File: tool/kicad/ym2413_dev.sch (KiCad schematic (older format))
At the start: 145 parts, among them J1 MICRO-USB-AB, K1 CONN_3, K2 CONN_3, P1 TEST_POINT, P10 TEST_POINT, P11 TEST_POINT, P12 TEST_POINT, P13 TEST_POINT, P14 TEST_POINT, P15 TEST_POINT, P16 TEST_POINT, P17 TEST_POINT, P18 TEST_POINT, P19 TEST_POINT, P2 TEST_POINT, P20 TEST_POINT, P21 TEST_POINT, P22 TEST_POINT, P23 TEST_POINT, P24 TEST_POINT, P25 TEST_POINT, P26 TEST_POINT, P27 TEST_POINT, P28 TEST_POINT, P29 TEST_POINT, P3 TEST_POINT, P30 CONN_3X2, P31 CONN_2, P32 CONN_2, P33 TEST_POINT, P34 TEST_POINT, P35 CONN_6, P37 TEST_POINT, P38 TEST_POINT, P4 TEST_POINT, P5 MIDI-IN, P6 TEST_POINT, P7 TEST_POINT, P8 TEST_POINT, P9 TEST_POINT, U1 SN74LVC2T45, U2 ST-USBLC6-2, U3 EFM32GG332, U4 YM2413, U5 LM386, U6 LM386, U7 ACPL-M21L, X1 48Mhz, X2 CRYSTAL

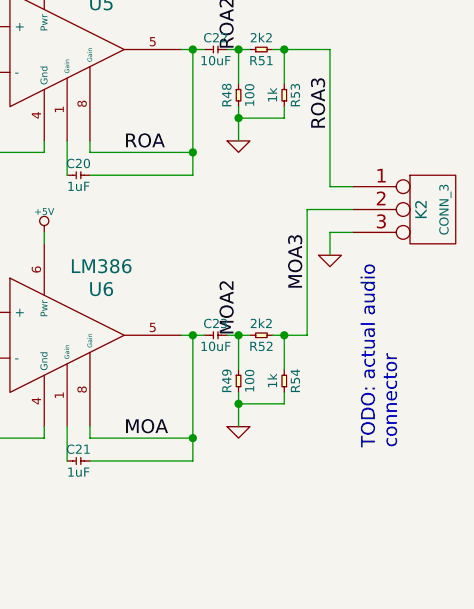
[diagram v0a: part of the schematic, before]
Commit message: fix audio footprint; add to board
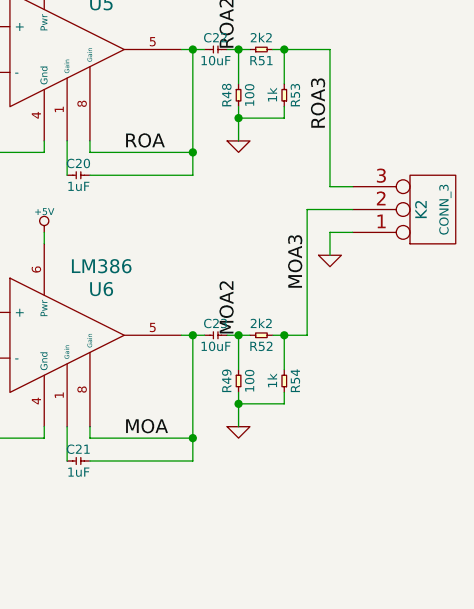
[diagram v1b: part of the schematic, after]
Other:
- note removed: "TODO: actual audio\nconnector"
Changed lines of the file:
@@
 F 3 "" H 10850 3950 60  0000 C CNN
 	1    10850 3950
-	1    0    0    -1
+	1    0    0    1
 $EndComp
 Wire Wire Line
@@
 Wire Wire Line
 	10400 4050 10400 4150
-Text Notes 10700 5000 1    60   ~ 0
-TODO: actual audio\nconnector
 $Comp
 L SN74LVC2T45 U1

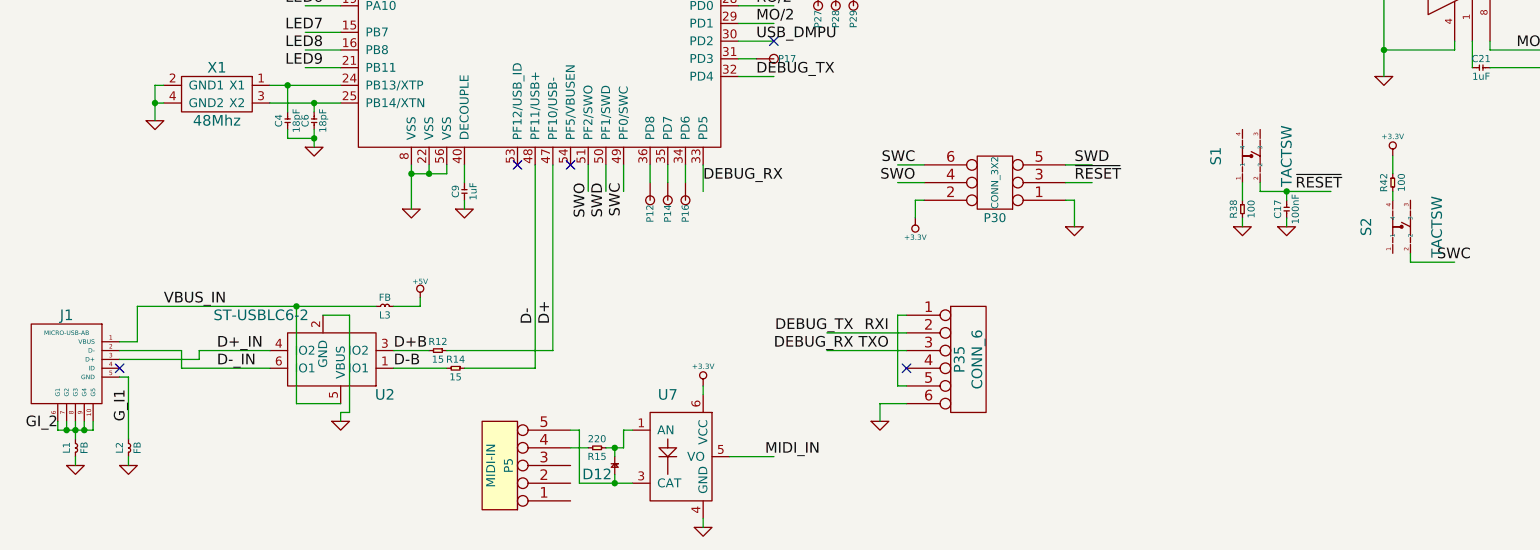
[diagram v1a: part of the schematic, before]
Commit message: ERC fixes
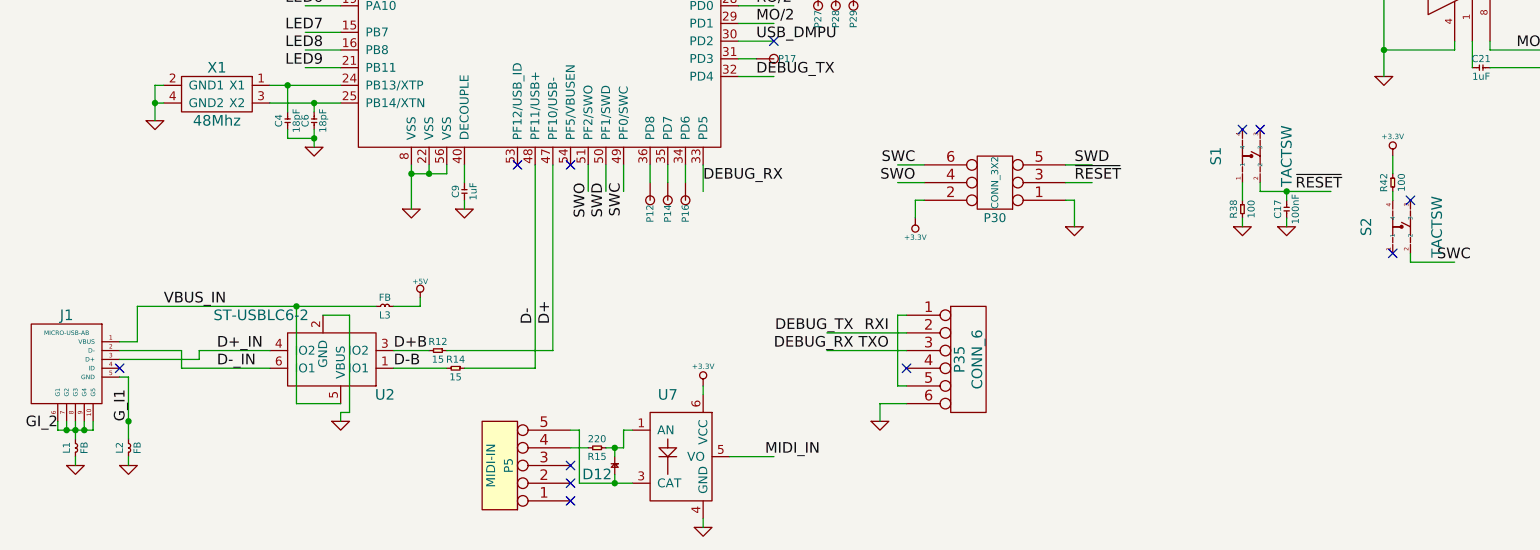
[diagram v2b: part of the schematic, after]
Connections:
- no-connect marks 5 -> 12
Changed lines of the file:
@@
 Wire Wire Line
 	5300 7250 5050 7250
+Connection ~ 1650 7050
+NoConn ~ 8800 6100
+NoConn ~ 8900 5800
+NoConn ~ 8050 5400
+NoConn ~ 7950 5400
+NoConn ~ 4150 7300
+NoConn ~ 4150 7400
+NoConn ~ 4150 7500
 $EndSCHEMATC

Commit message: work on 3V3 part
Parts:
- added C24: 4.7uF, symbol C
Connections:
- net labels added: DECOUPLE, SWCU, XTN, XTP, ~RESETD
- wire segments 356 -> 358
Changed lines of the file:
@@
 	4150 2550 4150 2500
 Wire Wire Line
-	4150 2500 4050 2500
+	4050 2500 4300 2500
 Connection ~ 4050 2500
 Wire Wire Line
@@
 NoConn ~ 4150 7400
 NoConn ~ 4150 7500
+Text Label 7950 5750 2    60   ~ 0
+~RESETD
+Text Label 8800 5800 2    60   ~ 0
+SWCU
+Text Label 2600 5150 0    60   ~ 0
+XTP
+Text Label 2600 5250 0    60   ~ 0
+XTN
+$Comp
+L C C24
+U 1 1 530648AC
+P 4300 2600
+F 0 "C24" H 4300 2650 40  0000 C CNN
+F 1 "4.7uF" H 4300 2550 40  0000 C CNN
+F 2 "" H 4300 2600 60  0000 C CNN
+F 3 "" H 4300 2600 60  0000 C CNN
+	1    4300 2600
+	0    -1   -1   0
+$EndComp
+Wire Wire Line
+	4300 2500 4300 2550
+Connection ~ 4150 2500
+$Comp
+L GND #PWR057
+U 1 1 53064A62
+P 4300 2700
+F 0 "#PWR057" H 4300 2700 30  0001 C CNN
+F 1 "GND" H 4300 2630 30  0001 C CNN
+F 2 "" H 4300 2700 60  0000 C CNN
+F 3 "" H 4300 2700 60  0000 C CNN
+	1    4300 2700
+	1    0    0    -1
+$EndComp
+Wire Wire Line
+	4300 2650 4300 2700
+Text Label 3550 5650 1    60   ~ 0
+DECOUPLE
 $EndSCHEMATC

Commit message: more layout work
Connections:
- net labels added: MOd2, ROd2
- net labels removed: MO/2, RO/2
- wire segments 358 -> 360
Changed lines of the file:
@@
 MO
 Text Label 9850 1600 0    60   ~ 0
-RO/2
+ROd2
 Text Label 9850 1700 0    60   ~ 0
-MO/2
+MOd2
 $Comp
 L R R40
@@
 	5300 4800 5100 4800
 Text Label 5200 4700 0    60   ~ 0
-RO/2
+ROd2
 Text Label 5200 4800 0    60   ~ 0
-MO/2
+MOd2
 Wire Wire Line
 	5300 4900 5100 4900
@@
 L GND #PWR050
 U 1 1 52F821C2
-P 4450 1200
-F 0 "#PWR050" H 4450 1200 30  0001 C CNN
-F 1 "GND" H 4450 1130 30  0001 C CNN
-F 2 "" H 4450 1200 60  0000 C CNN
-F 3 "" H 4450 1200 60  0000 C CNN
-	1    4450 1200
+P 4600 1200
+F 0 "#PWR050" H 4600 1200 30  0001 C CNN
+F 1 "GND" H 4600 1130 30  0001 C CNN
+F 2 "" H 4600 1200 60  0000 C CNN
+F 3 "" H 4600 1200 60  0000 C CNN
+	1    4600 1200
 	-1   0    0    1
 $EndComp
@@
 L +5V #PWR051
 U 1 1 52F821C8
-P 4350 1250
-F 0 "#PWR051" H 4350 1340 20  0001 C CNN
-F 1 "+5V" H 4350 1340 30  0000 C CNN
-F 2 "" H 4350 1250 60  0000 C CNN
-F 3 "" H 4350 1250 60  0000 C CNN
-	1    4350 1250
+P 4350 1200
+F 0 "#PWR051" H 4350 1290 20  0001 C CNN
+F 1 "+5V" H 4350 1290 30  0000 C CNN
+F 2 "" H 4350 1200 60  0000 C CNN
+F 3 "" H 4350 1200 60  0000 C CNN
+	1    4350 1200
 	1    0    0    -1
 $EndComp
@@
 L +3.3V #PWR052
 U 1 1 52F821CE
-P 4250 1250
-F 0 "#PWR052" H 4250 1210 30  0001 C CNN
-F 1 "+3.3V" H 4250 1360 30  0000 C CNN
-F 2 "" H 4250 1250 60  0000 C CNN
-F 3 "" H 4250 1250 60  0000 C CNN
-	1    4250 1250
+P 4100 1250
+F 0 "#PWR052" H 4100 1210 30  0001 C CNN
+F 1 "+3.3V" H 4100 1360 30  0000 C CNN
+F 2 "" H 4100 1250 60  0000 C CNN
+F 3 "" H 4100 1250 60  0000 C CNN
+	1    4100 1250
 	1    0    0    -1
 $EndComp
 Wire Wire Line
-	4450 1200 4450 1300
-Wire Wire Line
-	4350 1250 4350 1300
-Wire Wire Line
-	4250 1250 4250 1300
+	4350 1200 4350 1300
 $Comp
 L TEST_POINT P33
@@
 Text Label 3550 5650 1    60   ~ 0
 DECOUPLE
+Wire Wire Line
+	4450 1300 4600 1300
+Wire Wire Line
+	4600 1300 4600 1200
+Wire Wire Line
+	4250 1300 4250 1250
+Wire Wire Line
+	4250 1250 4100 1250
 $EndSCHEMATC

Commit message: finish first layout
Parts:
- removed D10, D11, D7, D8, D9: LED, symbol LED
- removed R10, R13, R7, R8, R9: 3k3, symbol R
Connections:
- wire segments 360 -> 345
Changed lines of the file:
@@
 	2750 1250 2750 1400
-$Comp
-L R R7
-U 1 1 52F7EF20
-P 2900 1450
-F 0 "R7" H 2900 1500 40  0000 C CNN
-F 1 "3k3" H 2900 1400 40  0000 C CNN
-F 2 "" H 2900 1450 60  0000 C CNN
-F 3 "" H 2900 1450 60  0000 C CNN
-	1    2900 1450
-	0    -1   -1   0
-$EndComp
-$Comp
-L LED D7
-U 1 1 52F7EF26
-P 2900 1650
-F 0 "D7" H 2900 1750 60  0000 C CNN
-F 1 "LED" H 2905 1585 60  0000 C CNN
-F 2 "" H 2900 1650 60  0000 C CNN
-F 3 "" H 2900 1650 60  0000 C CNN
-	1    2900 1650
-	0    1    1    0
-$EndComp
-Wire Wire Line
-	2900 1500 2900 1600
-Wire Wire Line
-	2900 1800 2900 1700
-$Comp
-L GND #PWR043
-U 1 1 52F7EF2E
-P 2900 1800
-F 0 "#PWR043" H 2900 1800 30  0001 C CNN
-F 1 "GND" H 2900 1730 30  0001 C CNN
-F 2 "" H 2900 1800 60  0000 C CNN
-F 3 "" H 2900 1800 60  0000 C CNN
-	1    2900 1800
-	1    0    0    -1
-$EndComp
-Wire Wire Line
-	2900 1250 2900 1400
-$Comp
-L R R8
-U 1 1 52F7EF35
-P 3050 1450
-F 0 "R8" H 3050 1500 40  0000 C CNN
-F 1 "3k3" H 3050 1400 40  0000 C CNN
-F 2 "" H 3050 1450 60  0000 C CNN
-F 3 "" H 3050 1450 60  0000 C CNN
-	1    3050 1450
-	0    -1   -1   0
-$EndComp
-$Comp
-L LED D8
-U 1 1 52F7EF3B
-P 3050 1650
-F 0 "D8" H 3050 1750 60  0000 C CNN
-F 1 "LED" H 3055 1585 60  0000 C CNN
-F 2 "" H 3050 1650 60  0000 C CNN
-F 3 "" H 3050 1650 60  0000 C CNN
-	1    3050 1650
-	0    1    1    0
-$EndComp
-Wire Wire Line
-	3050 1500 3050 1600
-Wire Wire Line
-	3050 1800 3050 1700
-$Comp
-L GND #PWR044
-U 1 1 52F7EF43
-P 3050 1800
-F 0 "#PWR044" H 3050 1800 30  0001 C CNN
-F 1 "GND" H 3050 1730 30  0001 C CNN
-F 2 "" H 3050 1800 60  0000 C CNN
-F 3 "" H 3050 1800 60  0000 C CNN
-	1    3050 1800
-	1    0    0    -1
-$EndComp
-Wire Wire Line
-	3050 1250 3050 1400
-$Comp
-L R R9
-U 1 1 52F7EF4A
-P 3200 1450
-F 0 "R9" H 3200 1500 40  0000 C CNN
-F 1 "3k3" H 3200 1400 40  0000 C CNN
-F 2 "" H 3200 1450 60  0000 C CNN
-F 3 "" H 3200 1450 60  0000 C CNN
-	1    3200 1450
-	0    -1   -1   0
-$EndComp
-$Comp
-L LED D9
-U 1 1 52F7EF50
-P 3200 1650
-F 0 "D9" H 3200 1750 60  0000 C CNN
-F 1 "LED" H 3205 1585 60  0000 C CNN
-F 2 "" H 3200 1650 60  0000 C CNN
-F 3 "" H 3200 1650 60  0000 C CNN
-	1    3200 1650
-	0    1    1    0
-$EndComp
-Wire Wire Line
-	3200 1500 3200 1600
-Wire Wire Line
-	3200 1800 3200 1700
-$Comp
-L GND #PWR045
-U 1 1 52F7EF58
-P 3200 1800
-F 0 "#PWR045" H 3200 1800 30  0001 C CNN
-F 1 "GND" H 3200 1730 30  0001 C CNN
-F 2 "" H 3200 1800 60  0000 C CNN
-F 3 "" H 3200 1800 60  0000 C CNN
-	1    3200 1800
-	1    0    0    -1
-$EndComp
-Wire Wire Line
-	3200 1250 3200 1400
-$Comp
-L GND #PWR046
-U 1 1 52F7EF5F
-P 3200 1800
-F 0 "#PWR046" H 3200 1800 30  0001 C CNN
-F 1 "GND" H 3200 1730 30  0001 C CNN
-F 2 "" H 3200 1800 60  0000 C CNN
-F 3 "" H 3200 1800 60  0000 C CNN
-	1    3200 1800
-	1    0    0    -1
-$EndComp
-$Comp
-L R R10
-U 1 1 52F7EF65
-P 3350 1450
-F 0 "R10" H 3350 1500 40  0000 C CNN
-F 1 "3k3" H 3350 1400 40  0000 C CNN
-F 2 "" H 3350 1450 60  0000 C CNN
-F 3 "" H 3350 1450 60  0000 C CNN
-	1    3350 1450
-	0    -1   -1   0
-$EndComp
-$Comp
-L LED D10
-U 1 1 52F7EF6B
-P 3350 1650
-F 0 "D10" H 3350 1750 60  0000 C CNN
-F 1 "LED" H 3355 1585 60  0000 C CNN
-F 2 "" H 3350 1650 60  0000 C CNN
-F 3 "" H 3350 1650 60  0000 C CNN
-	1    3350 1650
-	0    1    1    0
-$EndComp
-Wire Wire Line
-	3350 1500 3350 1600
-Wire Wire Line
-	3350 1800 3350 1700
-$Comp
-L GND #PWR047
-U 1 1 52F7EF73
-P 3350 1800
-F 0 "#PWR047" H 3350 1800 30  0001 C CNN
-F 1 "GND" H 3350 1730 30  0001 C CNN
-F 2 "" H 3350 1800 60  0000 C CNN
-F 3 "" H 3350 1800 60  0000 C CNN
-	1    3350 1800
-	1    0    0    -1
-$EndComp
-Wire Wire Line
-	3350 1250 3350 1400
-$Comp
-L R R13
-U 1 1 52F7EF7A
-P 3500 1450
-F 0 "R13" H 3500 1500 40  0000 C CNN
-F 1 "3k3" H 3500 1400 40  0000 C CNN
-F 2 "" H 3500 1450 60  0000 C CNN
-F 3 "" H 3500 1450 60  0000 C CNN
-	1    3500 1450
-	0    -1   -1   0
-$EndComp
-$Comp
-L LED D11
-U 1 1 52F7EF80
-P 3500 1650
-F 0 "D11" H 3500 1750 60  0000 C CNN
-F 1 "LED" H 3505 1585 60  0000 C CNN
-F 2 "" H 3500 1650 60  0000 C CNN
-F 3 "" H 3500 1650 60  0000 C CNN
-	1    3500 1650
-	0    1    1    0
-$EndComp
-Wire Wire Line
-	3500 1500 3500 1600
-Wire Wire Line
-	3500 1800 3500 1700
-$Comp
-L GND #PWR048
-U 1 1 52F7EF88
-P 3500 1800
-F 0 "#PWR048" H 3500 1800 30  0001 C CNN
-F 1 "GND" H 3500 1730 30  0001 C CNN
-F 2 "" H 3500 1800 60  0000 C CNN
-F 3 "" H 3500 1800 60  0000 C CNN
-	1    3500 1800
-	1    0    0    -1
-$EndComp
-Wire Wire Line
-	3500 1250 3500 1400
 $Comp
 L +5V #PWR049
@@
 Text Label 2750 1350 1    60   ~ 0
 LED4
-Text Label 2900 1350 1    60   ~ 0
-LED5
-Text Label 3050 1350 1    60   ~ 0
-LED6
-Text Label 3200 1350 1    60   ~ 0
-LED7
-Text Label 3350 1350 1    60   ~ 0
-LED8
-Text Label 3500 1350 1    60   ~ 0
-LED9
 Wire Wire Line
 	4900 5750 4900 5600

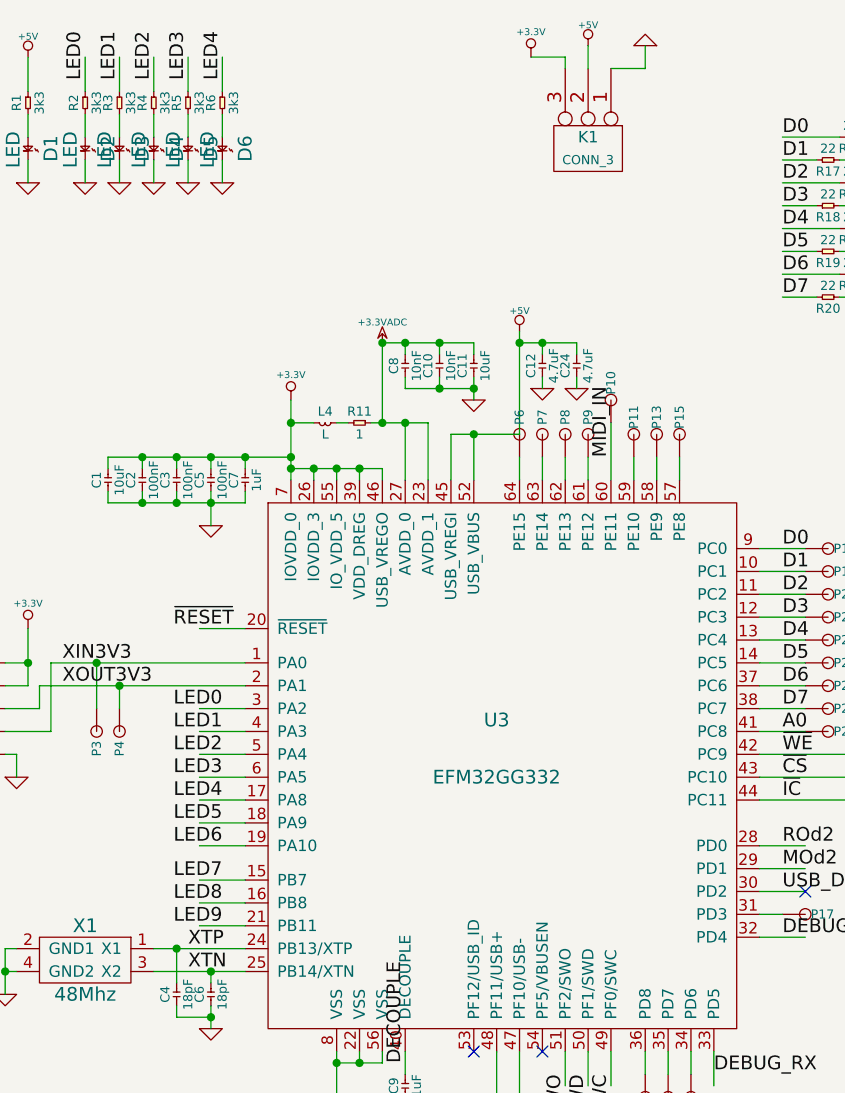
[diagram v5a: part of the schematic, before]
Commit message: re-add second 5 LEDs, but hook up to more reachable ports
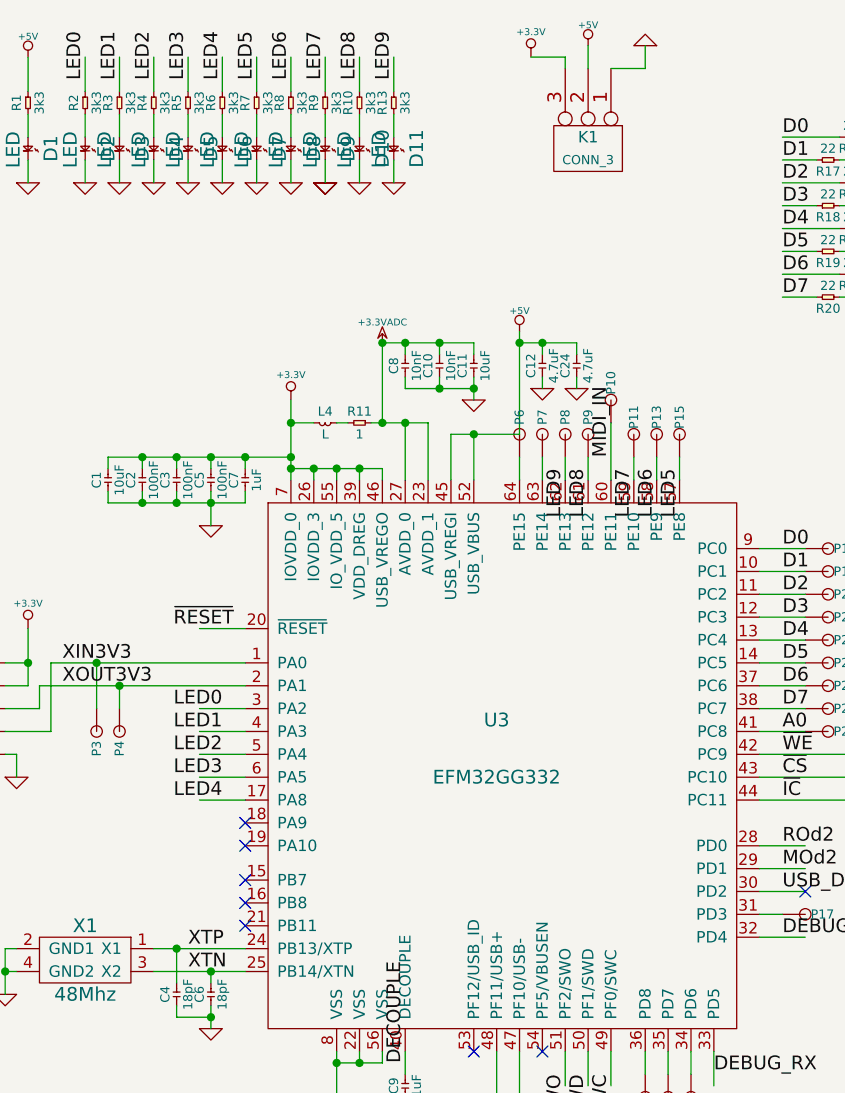
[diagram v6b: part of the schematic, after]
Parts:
- added D10, D11, D7, D8, D9: LED, symbol LED
- added R10, R13, R7, R8, R9: 3k3, symbol R
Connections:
- wire segments 345 -> 355
- no-connect marks 12 -> 17

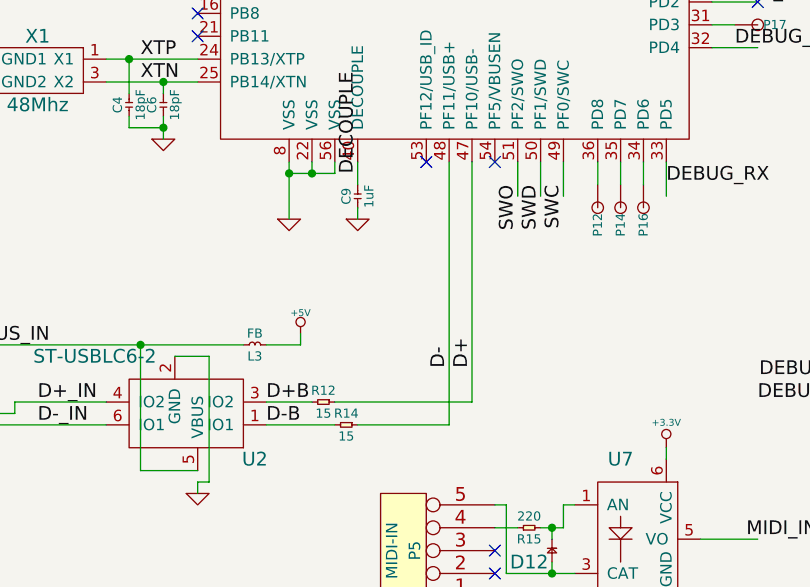
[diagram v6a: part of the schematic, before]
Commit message: fix D+ and D- in schematic
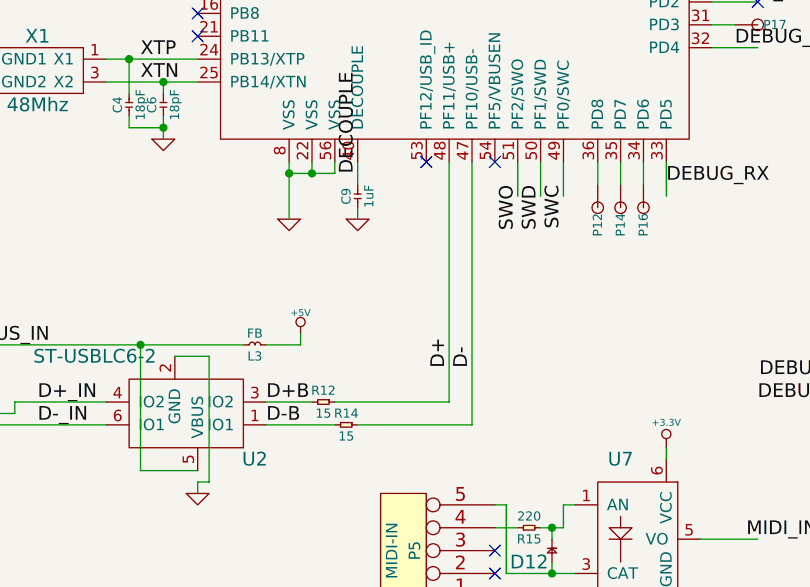
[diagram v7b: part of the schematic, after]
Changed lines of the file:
@@
 	1    0    0    -1
 $EndComp
+Text Label 4050 6500 1    60   ~ 0
+D-
 Text Label 3950 6500 1    60   ~ 0
-D-
-Text Label 4050 6500 1    60   ~ 0
 D+
 $Comp
@@
 	3850 2900 3850 3100
 Connection ~ 3850 2900
-Wire Wire Line
-	4050 6650 4050 5600
-Wire Wire Line
-	3950 6750 3950 5600
 Wire Wire Line
 	7300 3650 7300 3700
@@
 	2850 7000 2850 7050
 Wire Wire Line
-	3450 6650 4050 6650
-Wire Wire Line
-	3950 6750 3550 6750
+	3550 6750 4050 6750
 Wire Wire Line
 	2450 6650 2050 6650
@@
 NoConn ~ 2850 4950
 NoConn ~ 2850 5050
+Wire Wire Line
+	3450 6650 3950 6650
+Wire Wire Line
+	3950 6650 3950 5600
+Wire Wire Line
+	4050 6750 4050 5600
 $EndSCHEMATC
